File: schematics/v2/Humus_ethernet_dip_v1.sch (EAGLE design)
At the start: 31 parts, among them IC2 DS2432P

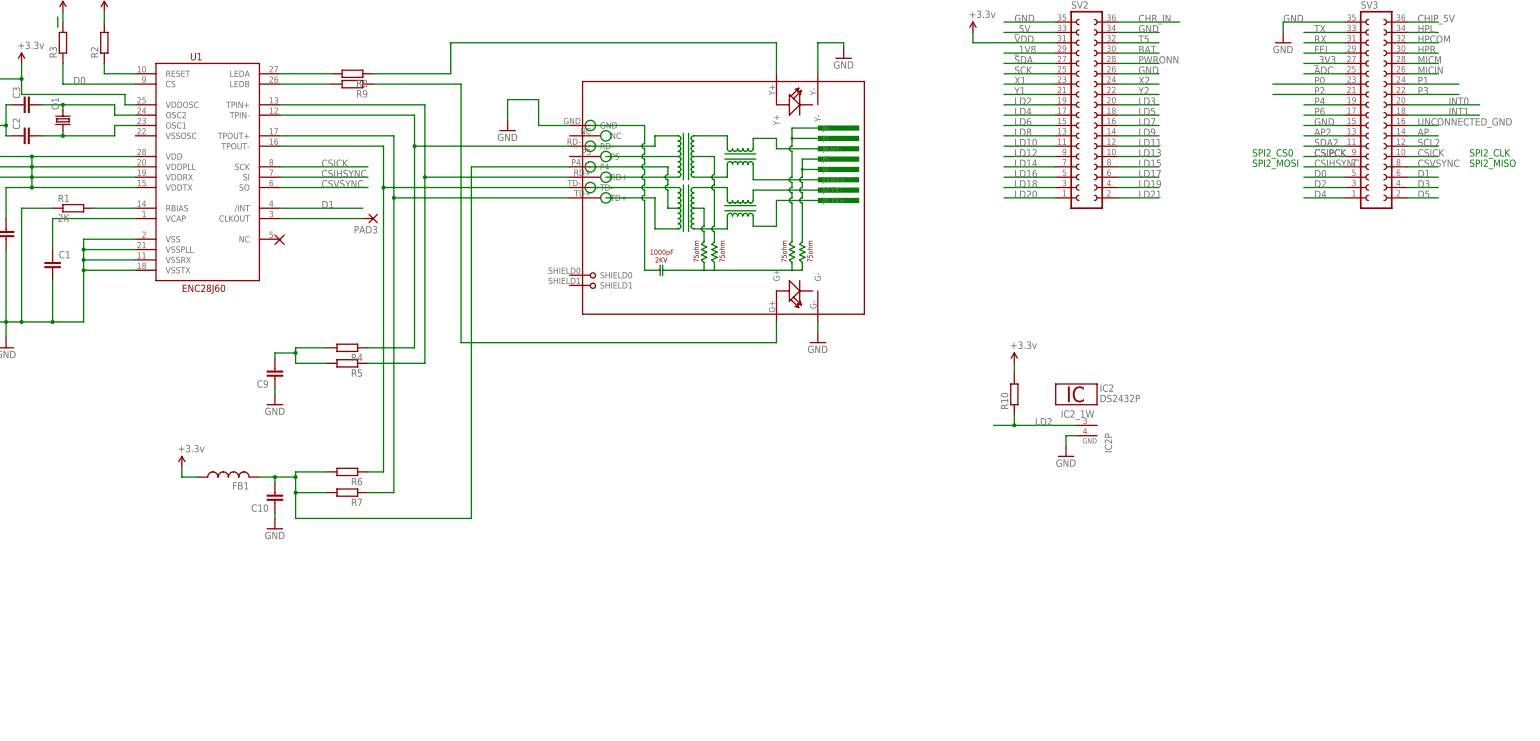
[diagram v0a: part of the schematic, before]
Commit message: added version two with EEPROM and DCDC
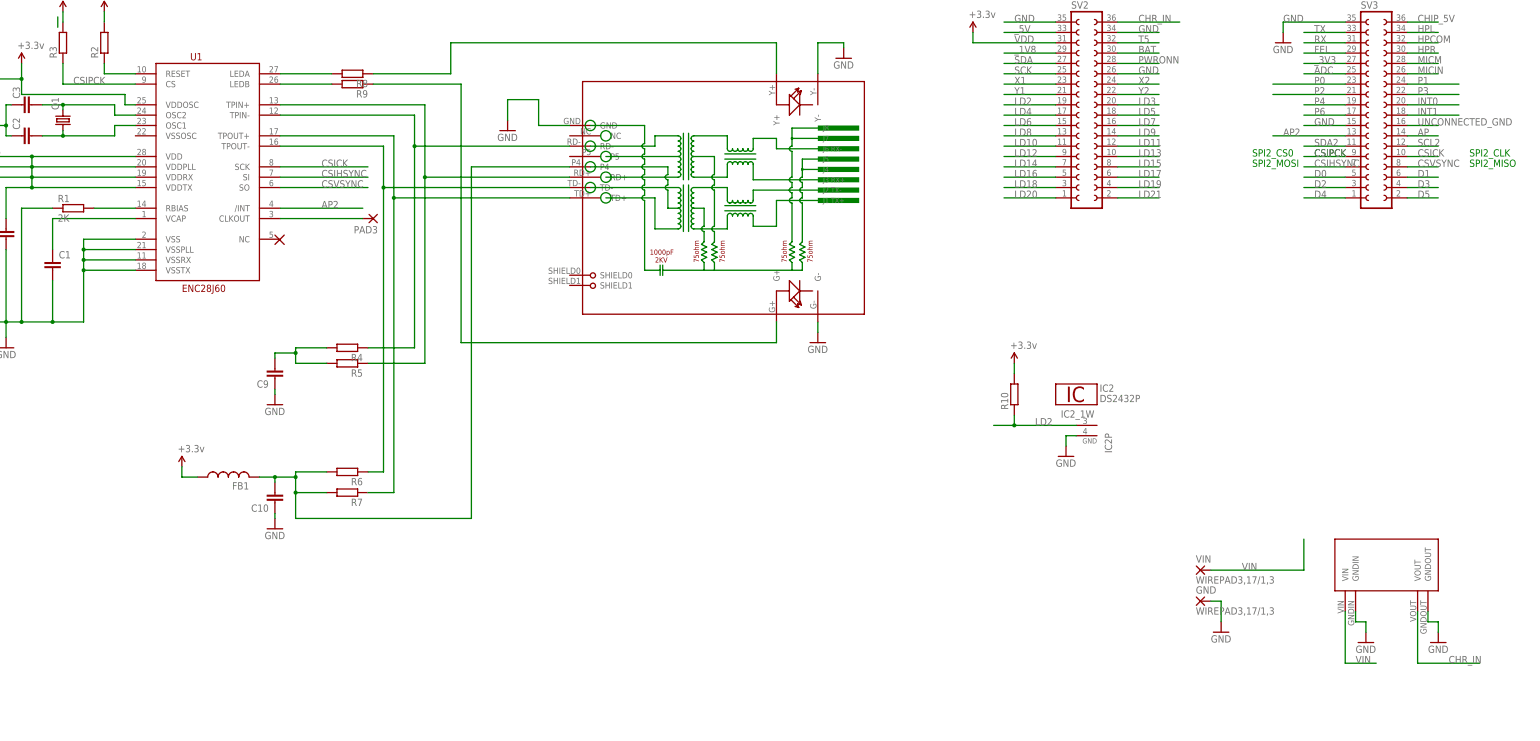
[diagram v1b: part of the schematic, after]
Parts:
- added GND, VIN: WIREPAD3,17/1,3, wirepad:WIREPAD3,17/1,3
- added U$9: MP1584EN_FRAMELESS, power_supply:MP1584EN_FRAMELESS
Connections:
- new net VIN: U$9.VIN, VIN.P
- net AP2: now also U1./INT
- net CHR_IN: now also U$9.VOUT
- net CSIPCK: now also R3.1, U1.CS
- net D0: no longer R3.1, U1.CS
- net D1: no longer U1./INT
- net GND: now also GND.P, U$9.GNDIN, U$9.GNDOUT
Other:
- note added: "Power"

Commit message: fixed connection
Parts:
- removed GND, VIN: WIREPAD3,17/1,3, wirepad:WIREPAD3,17/1,3
- removed R3: (no value), rcl:R-EU_R0805
- removed U$9: MP1584EN_FRAMELESS, power_supply:MP1584EN_FRAMELESS
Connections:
- removed net VIN: U$9.VIN, VIN.P
- net CHR_IN: no longer U$9.VOUT
- net CSIPCK: no longer R3.1
- net GND: no longer GND.P, U$9.GNDIN, U$9.GNDOUT
- net VDD: no longer R3.2
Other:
- note removed: "Power"
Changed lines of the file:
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@@
 <part name="C1" library="rcl" deviceset="C-EU" device="C0805"/>
 <part name="SUPPLY1" library="SparkFun-Aesthetics" deviceset="VDD" device="" value="+3.3v"/>
-<part name="SUPPLY2" library="SparkFun-Aesthetics" deviceset="VDD" device="" value="+3.3v"/>
 <part name="SUPPLY3" library="SparkFun-Aesthetics" deviceset="VDD" device="" value="+3.3v"/>
 <part name="R2" library="rcl" deviceset="R-EU_" device="R0805"/>
-<part name="R3" library="rcl" deviceset="R-EU_" device="R0805"/>
 <part name="Q1" library="adafruit" deviceset="CRYSTAL" device="SM49"/>
 <part name="SUPPLY4" library="SparkFun-Aesthetics" deviceset="VDD" device="" value="+3.3v"/>
@@
 <part name="R10" library="rcl" deviceset="R-EU_" device="R0805"/>
 <part name="SUPPLY7" library="SparkFun-Aesthetics" deviceset="VDD" device="" value="+3.3v"/>
-<part name="VIN" library="wirepad" deviceset="WIREPAD" device="3,17/1,3"/>
-<part name="GND" library="wirepad" deviceset="WIREPAD" device="3,17/1,3"/>
-<part name="U$9" library="power_supply" deviceset="MP1584EN_FRAMELESS" device=""/>
-<part name="GND4" library="supply1" deviceset="GND" device=""/>
-<part name="GND12" library="supply1" deviceset="GND" device=""/>
-<part name="GND13" library="supply1" deviceset="GND" device=""/>
 </parts>
 <sheets>
@@
 <text x="347.98" y="182.88" size="1.778" layer="91">SPI2_MOSI</text>
 <text x="401.32" y="182.88" size="1.778" layer="91">SPI2_MISO</text>
-<wire x1="411.48" y1="106.68" x2="327.66" y2="106.68" width="2.54" layer="103"/>
-<wire x1="327.66" y1="106.68" x2="327.66" y2="53.34" width="2.54" layer="103"/>
-<wire x1="327.66" y1="53.34" x2="411.48" y2="53.34" width="2.54" layer="103"/>
-<wire x1="411.48" y1="53.34" x2="411.48" y2="106.68" width="2.54" layer="103"/>
-<text x="330.2" y="96.52" size="5.08" layer="103">Power</text>
 </plain>
 <instances>
@@
 <instance part="C1" gate="G$1" x="53.34" y="160.02"/>
 <instance part="SUPPLY1" gate="VDD" x="26.67" y="190.5"/>
-<instance part="SUPPLY2" gate="VDD" x="55.88" y="220.98"/>
 <instance part="SUPPLY3" gate="VDD" x="66.04" y="220.98"/>
 <instance part="R2" gate="G$1" x="66.04" y="213.36" rot="R90"/>
-<instance part="R3" gate="G$1" x="55.88" y="213.36" rot="R90"/>
 <instance part="Q1" gate="G$1" x="55.88" y="194.31" rot="R90"/>
 <instance part="SUPPLY4" gate="VDD" x="45.72" y="208.28"/>
@@
 <instance part="R10" gate="G$1" x="289.56" y="127" rot="R90"/>
 <instance part="SUPPLY7" gate="VDD" x="289.56" y="134.62"/>
-<instance part="VIN" gate="G$1" x="335.28" y="83.82"/>
-<instance part="GND" gate="G$1" x="335.28" y="76.2"/>
-<instance part="U$9" gate="G$1" x="368.3" y="78.74"/>
-<instance part="GND4" gate="1" x="340.36" y="68.58"/>
-<instance part="GND12" gate="1" x="375.92" y="66.04"/>
-<instance part="GND13" gate="1" x="393.7" y="66.04"/>
 </instances>
 <busses>
@@
 <wire x1="302.26" y1="116.84" x2="302.26" y2="114.3" width="0.1524" layer="91"/>
 </segment>
-<segment>
-<pinref part="GND" gate="G$1" pin="P"/>
-<pinref part="GND4" gate="1" pin="GND"/>
-<wire x1="337.82" y1="76.2" x2="340.36" y2="76.2" width="0.1524" layer="91"/>
-<wire x1="340.36" y1="76.2" x2="340.36" y2="71.12" width="0.1524" layer="91"/>
-</segment>
-<segment>
-<pinref part="U$9" gate="G$1" pin="GNDIN"/>
-<wire x1="373.38" y1="73.66" x2="373.38" y2="71.12" width="0.1524" layer="91"/>
-<pinref part="GND12" gate="1" pin="GND"/>
-<wire x1="373.38" y1="71.12" x2="375.92" y2="71.12" width="0.1524" layer="91"/>
-<wire x1="375.92" y1="71.12" x2="375.92" y2="68.58" width="0.1524" layer="91"/>
-</segment>
-<segment>
-<pinref part="U$9" gate="G$1" pin="GNDOUT"/>
-<wire x1="391.16" y1="73.66" x2="391.16" y2="71.12" width="0.1524" layer="91"/>
-<pinref part="GND13" gate="1" pin="GND"/>
-<wire x1="391.16" y1="71.12" x2="393.7" y2="71.12" width="0.1524" layer="91"/>
-<wire x1="393.7" y1="71.12" x2="393.7" y2="68.58" width="0.1524" layer="91"/>
-</segment>
 </net>
 <net name="INT0" class="0">
 <segment>
-<label x="388.62" y="198.12" size="1.778" layer="95"/>
+<label x="396.24" y="198.12" size="1.778" layer="95"/>
 <pinref part="SV3" gate="G$1" pin="20"/>
-<wire x1="386.08" y1="198.12" x2="398.78" y2="198.12" width="0.1524" layer="91"/>
+<wire x1="386.08" y1="198.12" x2="403.86" y2="198.12" width="0.1524" layer="91"/>
 </segment>
 </net>
@@
 <segment>
 <pinref part="SV3" gate="G$1" pin="18"/>
-<wire x1="386.08" y1="195.58" x2="398.78" y2="195.58" width="0.1524" layer="91"/>
-<label x="388.62" y="195.58" size="1.778" layer="95"/>
+<wire x1="386.08" y1="195.58" x2="403.86" y2="195.58" width="0.1524" layer="91"/>
+<label x="396.24" y="195.58" size="1.778" layer="95"/>
 </segment>
 </net>
@@
 <segment>
 <pinref part="U1" gate="G$1" pin="CS"/>
-<pinref part="R3" gate="G$1" pin="1"/>
 <wire x1="73.66" y1="203.2" x2="55.88" y2="203.2" width="0.1524" layer="91"/>
-<wire x1="55.88" y1="203.2" x2="55.88" y2="208.28" width="0.1524" layer="91"/>
 <label x="58.42" y="203.2" size="1.778" layer="95"/>
 </segment>
@@
 <segment>
 <pinref part="SV3" gate="G$1" pin="13"/>
-<wire x1="370.84" y1="190.5" x2="353.06" y2="190.5" width="0.1524" layer="91"/>
-<label x="355.6" y="190.5" size="1.778" layer="95"/>
+<wire x1="370.84" y1="190.5" x2="360.68" y2="190.5" width="0.1524" layer="91"/>
+<label x="363.22" y="190.5" size="1.778" layer="95"/>
 </segment>
 <segment>
@@
 <pinref part="SV2" gate="G$1" pin="36"/>
 <label x="320.04" y="218.44" size="1.778" layer="95"/>
-</segment>
-<segment>
-<pinref part="U$9" gate="G$1" pin="VOUT"/>
-<wire x1="388.62" y1="73.66" x2="388.62" y2="60.96" width="0.1524" layer="91"/>
-<wire x1="388.62" y1="60.96" x2="403.86" y2="60.96" width="0.1524" layer="91"/>
-<label x="396.24" y="60.96" size="1.778" layer="95"/>
 </segment>
 </net>
@@
 </segment>
 <segment>
-<pinref part="R3" gate="G$1" pin="2"/>
-<pinref part="SUPPLY2" gate="VDD" pin="VDD"/>
-<wire x1="55.88" y1="218.44" x2="55.88" y2="220.98" width="0.1524" layer="91"/>
-</segment>
-<segment>
 <pinref part="U1" gate="G$1" pin="VDDOSC"/>
 <wire x1="73.66" y1="198.12" x2="71.12" y2="198.12" width="0.1524" layer="91"/>
@@
 </segment>
 <segment>
-<wire x1="54.61" y1="217.17" x2="54.61" y2="219.71" width="0.1524" layer="91"/>
-</segment>
-<segment>
 <pinref part="FB1" gate="G$1" pin="1"/>
 <pinref part="SUPPLY5" gate="VDD" pin="VDD"/>
@@
 </segment>
 </net>
-<net name="VIN" class="0">
-<segment>
-<pinref part="VIN" gate="G$1" pin="P"/>
-<wire x1="337.82" y1="83.82" x2="360.68" y2="83.82" width="0.1524" layer="91"/>
-<wire x1="360.68" y1="83.82" x2="360.68" y2="91.44" width="0.1524" layer="91"/>
-<label x="345.44" y="83.82" size="1.778" layer="95"/>
-</segment>
-<segment>
-<pinref part="U$9" gate="G$1" pin="VIN"/>
-<wire x1="370.84" y1="73.66" x2="370.84" y2="60.96" width="0.1524" layer="91"/>
-<wire x1="370.84" y1="60.96" x2="378.46" y2="60.96" width="0.1524" layer="91"/>
-<label x="373.38" y="60.96" size="1.778" layer="95"/>
-</segment>
-</net>
